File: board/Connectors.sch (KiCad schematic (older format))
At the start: 9 parts, among them J1 Conn_02x04_Counter_Clockwise, U2 TXB0106

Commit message: Clenaed up in and fixed some issues with the connectors sheet, adding the JTAG header and replacing the logic level translator with a more suitable set-direction suite
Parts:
- removed R3: 50k, rcl:R0603, symbol Device:R_Small
- removed U2: TXB0106, lethalbit:R-PVQFN-N16, symbol lethalbit:TXB0106
- added C4, C5: 0.1uF, rcl:C0603, symbol Device:C_Small
- added J2: Conn_02x05_Odd_Even_MountingPin, Connector_PinSocket_1.27mm:PinSocket_2x05_P1.27mm_Vertical_SMD, symbol Connector_Generic_MountingPin:Conn_02x05_Odd_Even_MountingPin
- added U2: FXL4TD245BQX, DX-MON:DQFN16_1EP_2.5x3.5mm_P0.5mm, symbol DX_MON:FXL4TD245BQX
- added U3: FXL2TD245L10X, DX-MON:MicroPack_1.6x2.1mm_P0.5mm, symbol DX_MON:FXL2TD245L10X
- R2: value 50k -> 10k
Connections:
- net labels added: SCK, TCK, TDI, TDO, TMS, ~SCS, ~SRST
- wire segments 53 -> 96

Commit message: Added the work to the schematic from the last stream, and updated all the footprints to reflect the work going in on my symbol and footprint libraries
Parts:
- removed C2, C3: 0.1uF, rcl:C0603, symbol Device:C_Small
- removed U3: FXL2TD245L10X, DX-MON:MicroPack_1.6x2.1mm_P0.5mm, symbol DX_MON:FXL2TD245L10X
- added D1: D_Schottky_Small, DX-MON:SOD882D_DFN1006D-2, symbol Device:D_Schottky_Small
- added Q1: DMN65D8L-7, rhais_package-smd:SOT-23, symbol Device:Q_NMOS_GSD
- C1, C4, C5: footprint rcl:C0603 -> rhais_rcl:C0603
- JP1: footprint USB:MICRO-USB-B-(IN_PCB) -> rhais_usb:MICRO-USB-B-(IN_PCB)
- R1, R2: footprint rcl:R0603 -> rhais_rcl:R0603
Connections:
- wire segments 96 -> 75
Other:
- note added: "JTAG"
- note added: "Logic Level Translation"
- note added: "USB"
- moved on the sheet: C1, C4, C5, J1, J2, JP1, R1, U2

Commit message: Added the two Flash devices and the user buttons to the schematic
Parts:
- J2: value Conn_02x05_Odd_Even_MountingPin -> Conn_02x05_Odd_Even; footprint Connector_PinSocket_1.27mm:PinSocket_2x05_P1.27mm_Vertical_SMD -> rhais_connector-pinheader:PinSocket_2x05_P1.27mm_Vertical_SMD; symbol Connector_Generic_MountingPin:Conn_02x05_Odd_Even_MountingPin -> Connector_Generic:Conn_02x05_Odd_Even
- U2: footprint DX-MON:DQFN16_1EP_2.5x3.5mm_P0.5mm -> rhais_package-qfn:DQFN16_1EP_2.5x3.5mm_P0.5mm
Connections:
- net GND: no longer J2.MP (MountPin)
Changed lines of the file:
@@
 $Descr A4 11693 8268
 encoding utf-8
-Sheet 2 4
+Sheet 2 5
 Title ""
 Date ""
@@
 F 0 "U2" H 7600 3050 50  0000 C CNN
 F 1 "FXL4TD245BQX" H 7500 1950 50  0000 C CNN
-F 2 "DX-MON:DQFN16_1EP_2.5x3.5mm_P0.5mm" H 7500 2500 50  0001 C CNN
+F 2 "rhais_package-qfn:DQFN16_1EP_2.5x3.5mm_P0.5mm" H 7500 2500 50  0001 C CNN
 F 3 "https://www.farnell.com/datasheets/2298347.pdf" H 7500 2500 50  0001 C CNN
 	1    7500 2500
@@
 	1    9500 1800
 	1    0    0    -1
-$EndComp
-$Comp
-L power:GND #PWR013
-U 1 1 5F512BAB
-P 2500 3000
-F 0 "#PWR013" H 2500 2750 50  0001 C CNN
-F 1 "GND" H 2505 2827 50  0000 C CNN
-F 2 "" H 2500 3000 50  0001 C CNN
-F 3 "" H 2500 3000 50  0001 C CNN
-	1    2500 3000
-	1    0    0    -1
-$EndComp
-Wire Wire Line
-	2500 2900 2500 3000
-$Comp
-L Connector_Generic_MountingPin:Conn_02x05_Odd_Even_MountingPin J2
-U 1 1 5F518617
-P 2550 2500
-F 0 "J2" H 2600 2917 50  0000 C CNN
-F 1 "Conn_02x05_Odd_Even_MountingPin" H 2600 2826 50  0000 C CNN
-F 2 "Connector_PinSocket_1.27mm:PinSocket_2x05_P1.27mm_Vertical_SMD" H 2550 2500 50  0001 C CNN
-F 3 "~" H 2550 2500 50  0001 C CNN
-	1    2550 2500
-	-1   0    0    -1
 $EndComp
 Text HLabel 2150 2300 0    39   Output ~ 0
@@
 Text HLabel 2150 2600 0    39   Output ~ 0
 TDI
+$Comp
+L Connector_Generic:Conn_02x05_Odd_Even J2
+U 1 1 5F518617
+P 2550 2500
+F 0 "J2" H 2600 2917 50  0000 C CNN
+F 1 "Conn_02x05_Odd_Even" H 2600 2826 50  0000 C CNN
+F 2 "rhais_connector-pinheader:PinSocket_2x05_P1.27mm_Vertical_SMD" H 2550 2500 50  0001 C CNN
+F 3 "~" H 2550 2500 50  0001 C CNN
+	1    2550 2500
+	-1   0    0    -1
+$EndComp
 $EndSCHEMATC

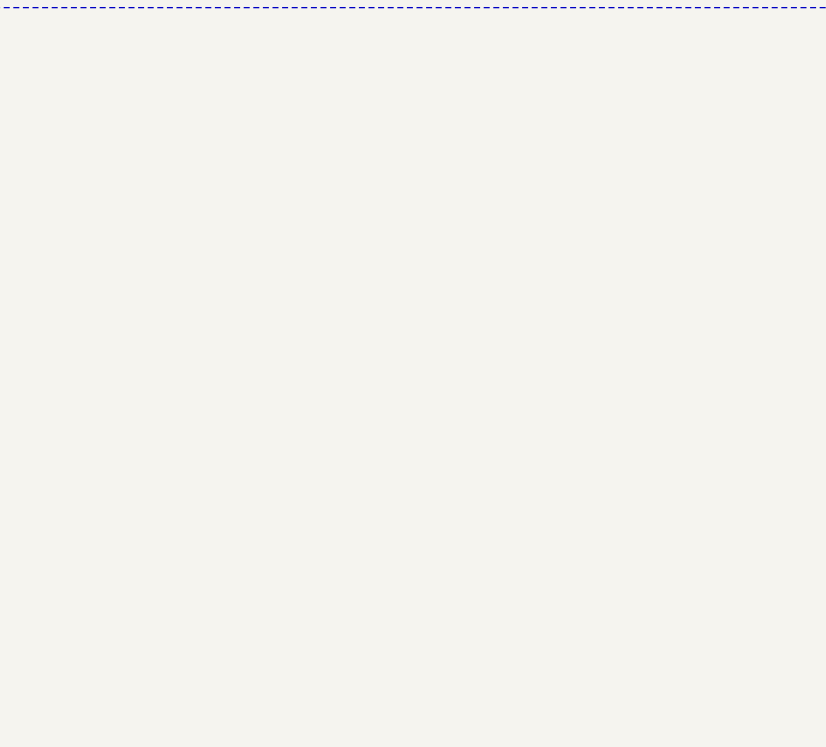
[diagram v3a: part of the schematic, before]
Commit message: Added the power LED for the target I missed
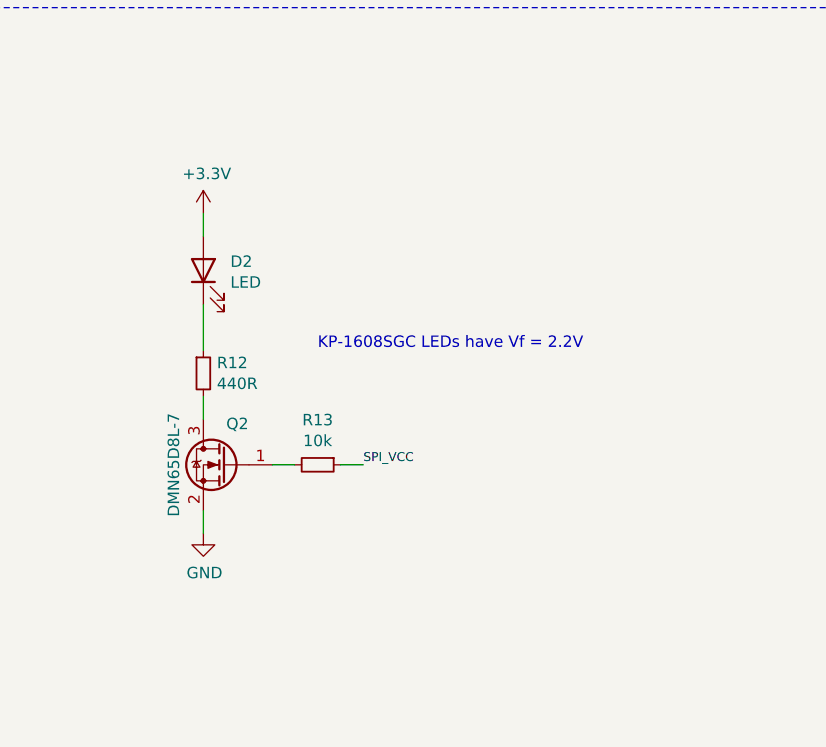
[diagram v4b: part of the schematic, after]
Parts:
- added D2: LED, rhais_led:LED0603, symbol Device:LED
- added Q2: DMN65D8L-7, rhais_package-smd:SOT-23, symbol Device:Q_NMOS_GSD
- added R12: 440R, rhais_rcl:R0603, symbol Device:R_Small
- added R13: 10k, rhais_rcl:R0603, symbol Device:R_Small
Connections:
- net +3V3: now also D2.2 (A)
- net GND: now also Q2.2 (S)
- net SPI_VCC: now also R13.1
- new net: D2.1 (K), R12.1
- new net: Q2.3 (D), R12.2
- new net: Q2.1 (G), R13.2
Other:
- note added: "KP-1608SGC LEDs have Vf = 2.2V"
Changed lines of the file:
@@
 	-1   0    0    -1
 $EndComp
+$Comp
+L Device:R_Small R?
+U 1 1 5F95430B
+P 6000 5600
+AR Path="/5F6E308F/5F95430B" Ref="R?"  Part="1"
+AR Path="/5F0A82B6/5F95430B" Ref="R12"  Part="1"
+F 0 "R12" H 6059 5646 50  0000 L CNN
+F 1 "440R" H 6059 5555 50  0000 L CNN
+F 2 "rhais_rcl:R0603" H 6000 5600 50  0001 C CNN
+F 3 "http://www.farnell.com/datasheets/2860681.pdf" H 6000 5600 50  0001 C CNN
+F 4 "Multicomp" H 6000 5600 50  0001 C CNN "MFR"
+F 5 "MCWR06X4700FTL" H 6000 5600 50  0001 C CNN "MPN"
+F 6 "2447374" H 6000 5600 50  0001 C CNN "OC_FARNELL"
+F 7 "https://uk.farnell.com/multicomp/mcwr06x4700ftl/res-470r-1-0-1w-0603-thick-film/dp/2447374" H 6000 5600 50  0001 C CNN "URL_FARNELL"
+	1    6000 5600
+	1    0    0    -1
+$EndComp
+$Comp
+L Device:LED D?
+U 1 1 5F954311
+P 6000 5150
+AR Path="/5F6E308F/5F954311" Ref="D?"  Part="1"
+AR Path="/5F0A82B6/5F954311" Ref="D2"  Part="1"
+F 0 "D2" V 6039 5032 50  0000 R CNN
+F 1 "LED" V 5948 5032 50  0000 R CNN
+F 2 "rhais_led:LED0603" H 6000 5150 50  0001 C CNN
+F 3 "https://www.kingbright.com/attachments/file/psearch/000/00/20160808bak/KP-1608SGC(Ver.21B).pdf" H 6000 5150 50  0001 C CNN
+F 4 "8529833" V 6000 5150 50  0001 C CNN "OC_FARNELL"
+F 5 "https://uk.farnell.com/kingbright/kp-1608sgc/led-0-8mm-x-1-2mm-green-12mcd/dp/8529833" V 6000 5150 50  0001 C CNN "URL_FARNELL"
+F 6 "Kingbright" H 6000 5150 50  0001 C CNN "MFR"
+F 7 "KP-1608SGC" H 6000 5150 50  0001 C CNN "MPN"
+	1    6000 5150
+	0    -1   -1   0
+$EndComp
+$Comp
+L power:+3.3V #PWR?
+U 1 1 5F954317
+P 6000 4900
+AR Path="/5F6E308F/5F954317" Ref="#PWR?"  Part="1"
+AR Path="/5F0A82B6/5F954317" Ref="#PWR038"  Part="1"
+F 0 "#PWR038" H 6000 4750 50  0001 C CNN
+F 1 "+3.3V" H 6015 5073 50  0000 C CNN
+F 2 "" H 6000 4900 50  0001 C CNN
+F 3 "" H 6000 4900 50  0001 C CNN
+	1    6000 4900
+	1    0    0    -1
+$EndComp
+Wire Wire Line
+	6000 4900 6000 5000
+Wire Wire Line
+	6000 5300 6000 5500
+$Comp
+L power:GND #PWR?
+U 1 1 5F95431F
+P 6000 6300
+AR Path="/5F6E308F/5F95431F" Ref="#PWR?"  Part="1"
+AR Path="/5F0A82B6/5F95431F" Ref="#PWR039"  Part="1"
+F 0 "#PWR039" H 6000 6050 50  0001 C CNN
+F 1 "GND" H 6005 6127 50  0000 C CNN
+F 2 "" H 6000 6300 50  0001 C CNN
+F 3 "" H 6000 6300 50  0001 C CNN
+	1    6000 6300
+	1    0    0    -1
+$EndComp
+Wire Wire Line
+	6000 5700 6000 5800
+Text Label 6700 6000 0    39   ~ 0
+SPI_VCC
+$Comp
+L Device:Q_NMOS_GSD Q2
+U 1 1 5F958118
+P 6100 6000
+F 0 "Q2" H 6100 6150 50  0000 R BNN
+F 1 "DMN65D8L-7" V 6300 6000 50  0000 C TNN
+F 2 "rhais_package-smd:SOT-23" H 6300 6100 50  0001 C CNN
+F 3 "https://www.farnell.com/datasheets/2040106.pdf" H 6100 6000 50  0001 C CNN
+	1    6100 6000
+	-1   0    0    -1
+$EndComp
+Wire Wire Line
+	6000 6300 6000 6200
+$Comp
+L Device:R_Small R?
+U 1 1 5F964FD0
+P 6500 6000
+AR Path="/5F6E308F/5F964FD0" Ref="R?"  Part="1"
+AR Path="/5F0A82B6/5F964FD0" Ref="R13"  Part="1"
+F 0 "R13" V 6304 6000 50  0000 C CNN
+F 1 "10k" V 6395 6000 50  0000 C CNN
+F 2 "rhais_rcl:R0603" H 6500 6000 50  0001 C CNN
+F 3 "~" H 6500 6000 50  0001 C CNN
+	1    6500 6000
+	0    1    1    0
+$EndComp
+Wire Wire Line
+	6300 6000 6400 6000
+Wire Wire Line
+	6700 6000 6600 6000
+Text Notes 6500 5500 0    50   ~ 0
+KP-1608SGC LEDs have Vf = 2.2V
 $EndSCHEMATC

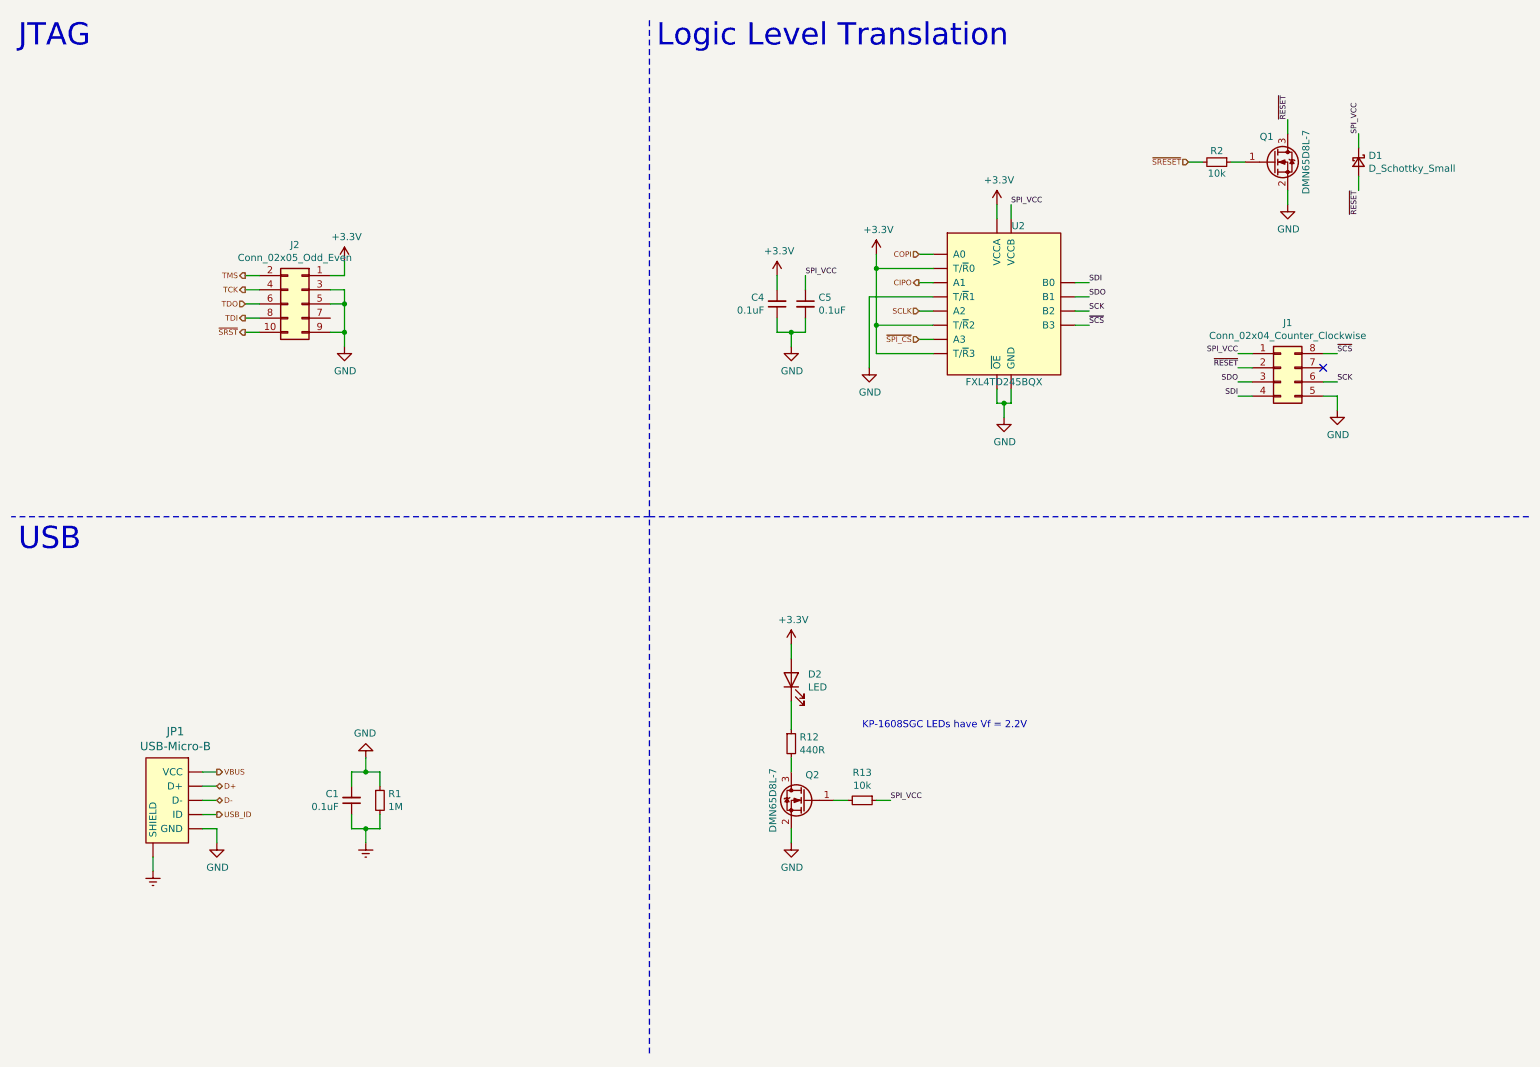
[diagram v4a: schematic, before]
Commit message: Cleanup and fixes for ERC errors
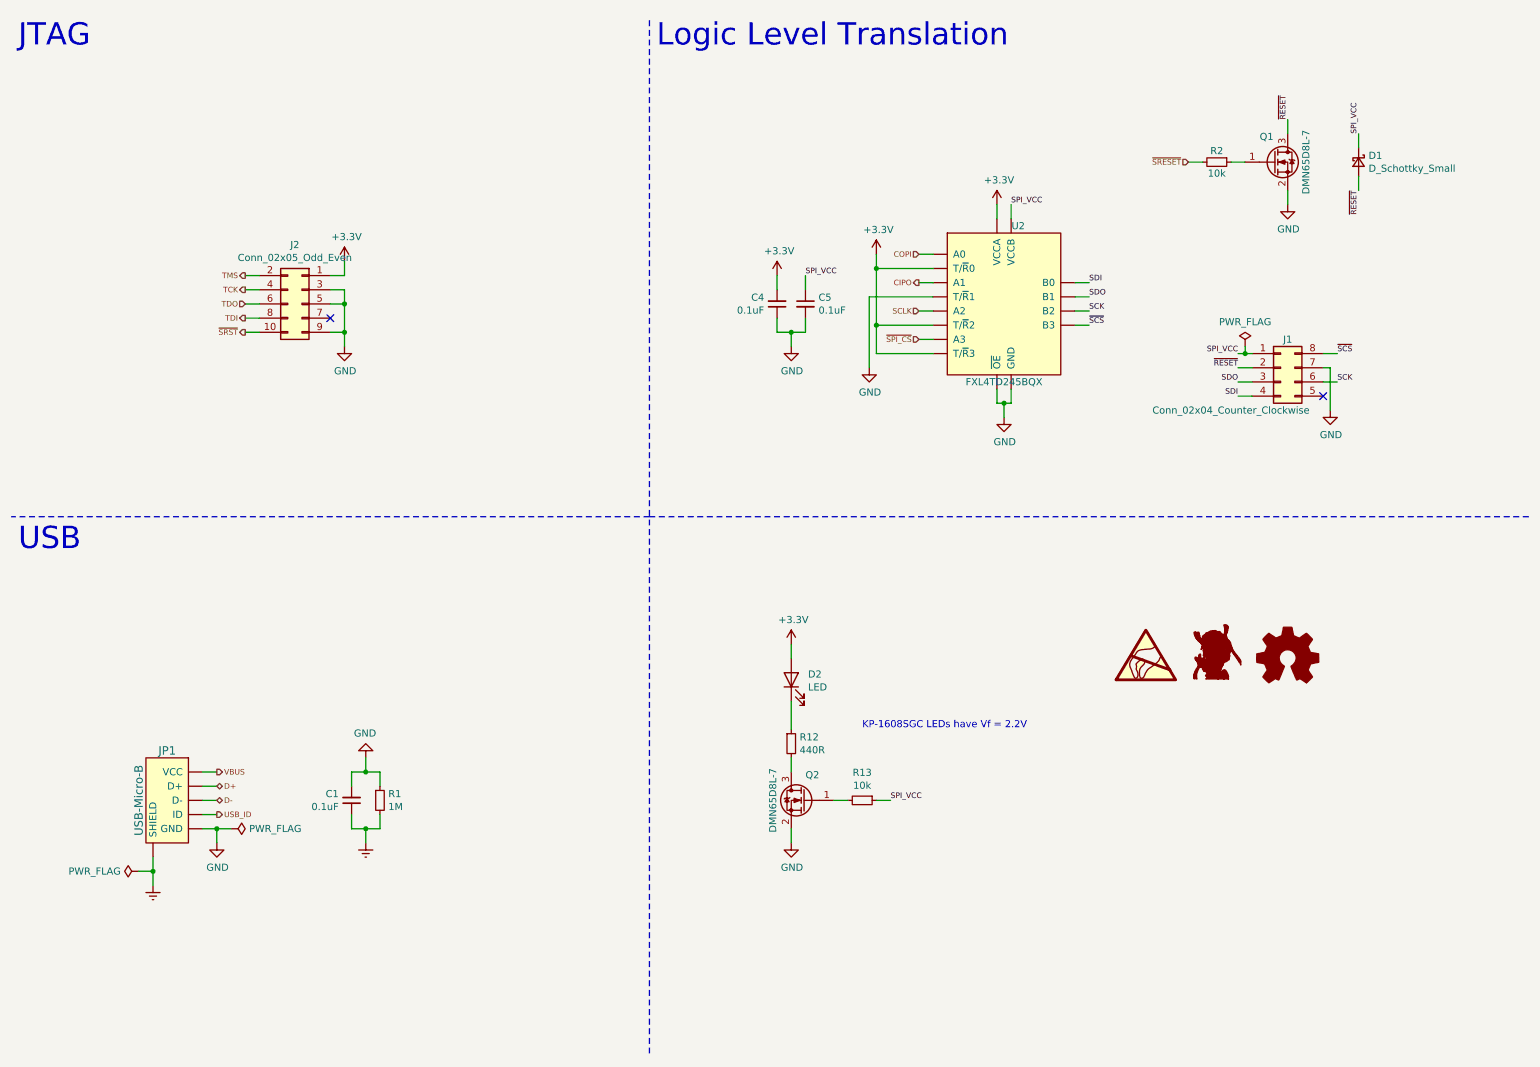
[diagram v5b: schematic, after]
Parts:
- added DRG1: トール, トール:トール-8.6x9.9, symbol DX_MON:トール
- added LOGO1: Logo_Open_Hardware_Small, Symbol:OSHW-Symbol_6.7x6mm_SilkScreen, symbol Graphic:Logo_Open_Hardware_Small
- added SYM1: SYM_ESD_Small, Symbol:WEEE-Logo_4.2x6mm_SilkScreen, symbol Graphic:SYM_ESD_Large
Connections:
- net GND: now also J1.7 (Pin_7); no longer J1.5 (Pin_5)
- no-connect marks 1 -> 2
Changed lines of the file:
@@
 U 1 1 5F0E0772
 P 1600 6000
-F 0 "JP1" H 1658 6486 59  0000 C CNN
-F 1 "USB-Micro-B" H 1658 6381 59  0000 C CNN
+F 0 "JP1" H 1600 6350 59  0000 C CNN
+F 1 "USB-Micro-B" V 1400 6000 59  0000 C CNN
 F 2 "rhais_usb:MICRO-USB-B-(IN_PCB)" H 1650 6000 59  0001 C CNN
 F 3 "" H 1650 6000 59  0001 C CNN
@@
 VBUS
 Wire Wire Line
-	1850 5800 1950 5800
-Wire Wire Line
 	1950 5900 1850 5900
 Wire Wire Line
@@
 L power:Earth #PWR01
 U 1 1 5F0E1C30
-P 1500 6500
-F 0 "#PWR01" H 1500 6250 50  0001 C CNN
-F 1 "Earth" H 1500 6350 50  0001 C CNN
-F 2 "" H 1500 6500 50  0001 C CNN
-F 3 "~" H 1500 6500 50  0001 C CNN
-	1    1500 6500
+P 1500 6600
+F 0 "#PWR01" H 1500 6350 50  0001 C CNN
+F 1 "Earth" H 1500 6450 50  0001 C CNN
+F 2 "" H 1500 6600 50  0001 C CNN
+F 3 "~" H 1500 6600 50  0001 C CNN
+	1    1500 6600
 	1    0    0    -1
 $EndComp
@@
 L power:GND #PWR09
 U 1 1 5F0F1067
-P 9850 3250
-F 0 "#PWR09" H 9850 3000 50  0001 C CNN
-F 1 "GND" H 9855 3077 50  0000 C CNN
-F 2 "" H 9850 3250 50  0001 C CNN
-F 3 "" H 9850 3250 50  0001 C CNN
-	1    9850 3250
-	1    0    0    -1
-$EndComp
-Text Label 9150 2850 2    39   ~ 0
-SPI_VCC
+P 9800 3250
+F 0 "#PWR09" H 9800 3000 50  0001 C CNN
+F 1 "GND" H 9805 3077 50  0000 C CNN
+F 2 "" H 9800 3250 50  0001 C CNN
+F 3 "" H 9800 3250 50  0001 C CNN
+	1    9800 3250
+	1    0    0    -1
+$EndComp
 $Comp
 L Connector_Generic:Conn_02x04_Counter_Clockwise J1
 U 1 1 5F0F1F73
 P 9450 2950
-F 0 "J1" H 9500 3267 50  0000 C CNN
-F 1 "Conn_02x04_Counter_Clockwise" H 9500 3176 50  0000 C CNN
+F 0 "J1" H 9500 3150 50  0000 C CNN
+F 1 "Conn_02x04_Counter_Clockwise" H 9100 2650 50  0000 C CNN
 F 2 "DX-MON:75867-132LF" H 9450 2950 50  0001 C CNN
 F 3 "~" H 9450 2950 50  0001 C CNN
@@
 Text Label 9150 2950 2    39   ~ 0
 ~RESET
-Wire Wire Line
-	9150 2850 9250 2850
 Wire Wire Line
 	9250 2950 9150 2950
@@
 	9850 2850 9750 2850
 Wire Wire Line
-	9750 3150 9850 3150
-Wire Wire Line
-	9850 3150 9850 3250
-NoConn ~ 9750 2950
+	9750 2950 9800 2950
+Wire Wire Line
+	9800 2950 9800 3250
 Wire Wire Line
 	6900 2150 7000 2150
@@
 Text Notes 6500 5500 0    50   ~ 0
 KP-1608SGC LEDs have Vf = 2.2V
+$Comp
+L DX_MON:トール DRG1
+U 1 1 5F92053D
+P 9000 4950
+F 0 "DRG1" H 9000 4786 60  0001 C CNN
+F 1 "トール" H 9000 5114 60  0001 C CNN
+F 2 "トール:トール-8.6x9.9" H 9000 4950 59  0001 C CNN
+F 3 "" H 9000 4950 59  0001 C CNN
+	1    9000 4950
+	1    0    0    -1
+$EndComp
+NoConn ~ 9750 3150
+Wire Wire Line
+	9150 2850 9200 2850
+Text Label 9150 2850 2    39   ~ 0
+SPI_VCC
+$Comp
+L Graphic:Logo_Open_Hardware_Small LOGO1
+U 1 1 5F9593C0
+P 9500 5000
+F 0 "LOGO1" H 9500 5275 50  0001 C CNN
+F 1 "Logo_Open_Hardware_Small" H 9500 4775 50  0001 C CNN
+F 2 "Symbol:OSHW-Symbol_6.7x6mm_SilkScreen" H 9500 5000 50  0001 C CNN
+F 3 "~" H 9500 5000 50  0001 C CNN
+	1    9500 5000
+	1    0    0    -1
+$EndComp
+$Comp
+L Graphic:SYM_ESD_Large SYM1
+U 1 1 5F95A3AC
+P 8500 4950
+F 0 "SYM1" H 8500 5090 50  0001 C CNN
+F 1 "SYM_ESD_Small" H 8500 4825 50  0001 C CNN
+F 2 "Symbol:WEEE-Logo_4.2x6mm_SilkScreen" H 8500 4960 50  0001 C CNN
+F 3 "~" H 8500 4960 50  0001 C CNN
+	1    8500 4950
+	1    0    0    -1
+$EndComp
+NoConn ~ 2750 2600
+$Comp
+L power:PWR_FLAG #FLG0101
+U 1 1 5F981A08
+P 9200 2800
+F 0 "#FLG0101" H 9200 2875 50  0001 C CNN
+F 1 "PWR_FLAG" H 9200 2973 50  0000 C CNN
+F 2 "" H 9200 2800 50  0001 C CNN
+F 3 "~" H 9200 2800 50  0001 C CNN
+	1    9200 2800
+	1    0    0    -1
+$EndComp
+Connection ~ 9200 2850
+Wire Wire Line
+	9200 2850 9250 2850
+Wire Wire Line
+	9200 2800 9200 2850
+$Comp
+L power:PWR_FLAG #FLG01
+U 1 1 5F985DB3
+P 2050 6200
+F 0 "#FLG01" H 2050 6275 50  0001 C CNN
+F 1 "PWR_FLAG" V 2050 6328 50  0000 L CNN
+F 2 "" H 2050 6200 50  0001 C CNN
+F 3 "~" H 2050 6200 50  0001 C CNN
+	1    2050 6200
+	0    1    1    0
+$EndComp
+Wire Wire Line
+	1950 6200 2050 6200
+Connection ~ 1950 6200
+Wire Wire Line
+	1850 5800 1950 5800
+$Comp
+L power:PWR_FLAG #FLG0102
+U 1 1 5F98CEF3
+P 1400 6500
+F 0 "#FLG0102" H 1400 6575 50  0001 C CNN
+F 1 "PWR_FLAG" V 1400 6627 50  0000 L CNN
+F 2 "" H 1400 6500 50  0001 C CNN
+F 3 "~" H 1400 6500 50  0001 C CNN
+	1    1400 6500
+	0    -1   -1   0
+$EndComp
+Wire Wire Line
+	1400 6500 1500 6500
+Connection ~ 1500 6500
+Wire Wire Line
+	1500 6500 1500 6600
 $EndSCHEMATC
